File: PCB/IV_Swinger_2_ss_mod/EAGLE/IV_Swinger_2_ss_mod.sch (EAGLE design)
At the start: 33 parts, among them J1 

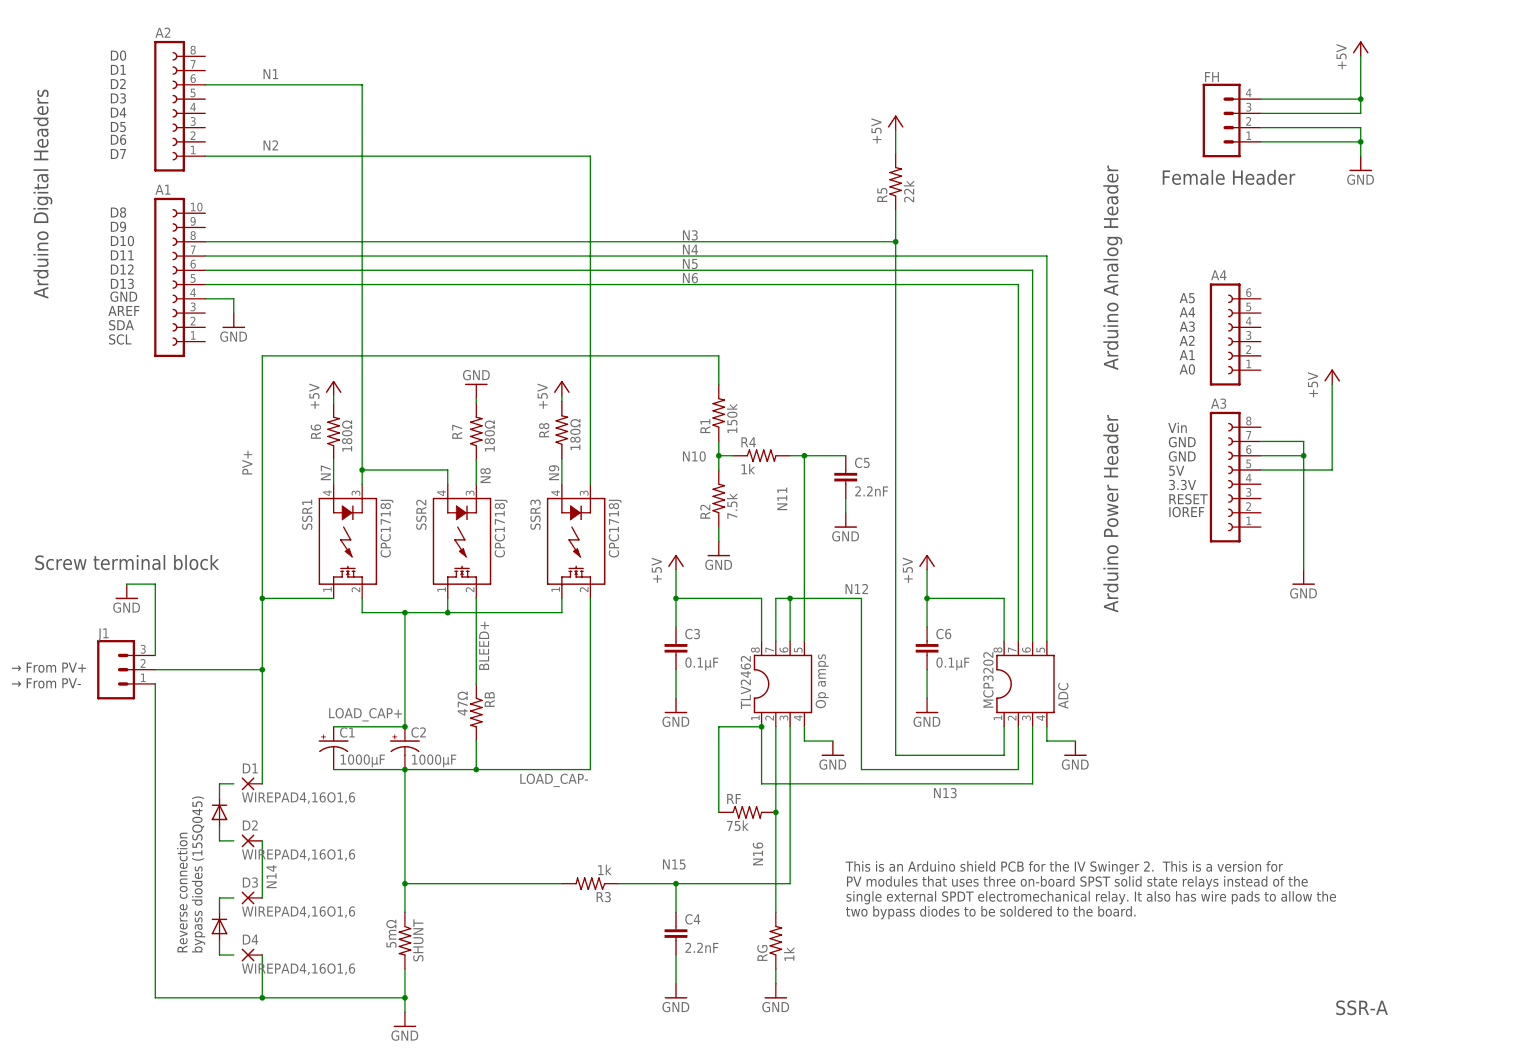
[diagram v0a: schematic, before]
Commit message: SSR module version PCB, RevB
Fixed bugs in RevA of the SSR module version PCB:

Issue #40: Must drive SSR1 and SSR2 from separate Arduino pins. In the RevA design, there is a path from +5V to GND through the two SSRs, which can cause destruction of the SSRs and the bleed resistor.

Issue #41: Resistor R3 must be connected precisely to the shunt (+) end pad so it doesn't see the voltage at some point in the sea of copper that is the LOAD_CAP- net.  This resulted in current measurements that were too high, and depended on whether the current was flowing from SSR3 or from the load caps.

Issue #41: The path from the shunt (-) end pad to the screw terminal pads must be a stub off the GND plane so that when current is flowing, the GND plane doesn't see a voltage drop.  Also, the linkage between this stub and the GND plane must be made at the shunt (-) end pad so the voltage of the GND plane is equal to the voltage at the (-) end of the shunt.

Also swapped the pads for the bypass diodes for layout reasons related to making the current-carrying part of GND a stub.
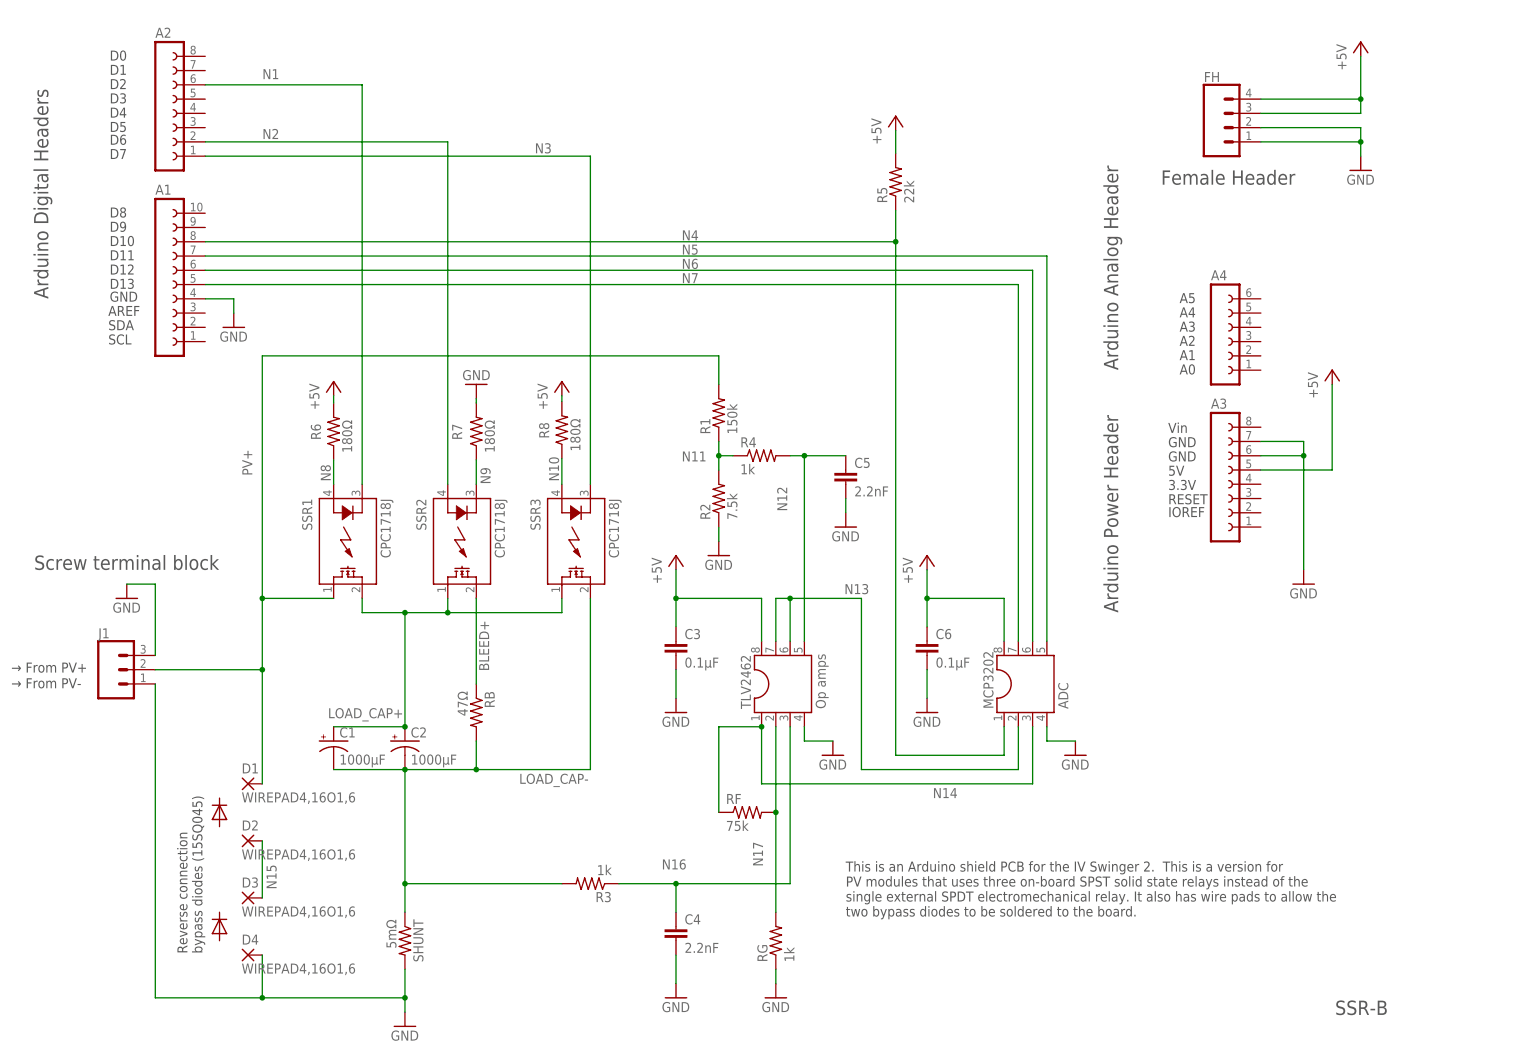
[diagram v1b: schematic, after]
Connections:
- new net N17: RF.2, RG.2, TLV2462.2
- net N1: no longer SSR2.A
- net N10: now also R8.1, SSR3.A; no longer R1.1, R2.2, R4.1
- net N11: now also R1.1, R2.2, R4.1; no longer C5.1, R4.2, TLV2462.5
- net N12: now also C5.1, R4.2, TLV2462.5; no longer MCP3202.2, TLV2462.6, TLV2462.7
- net N13: now also MCP3202.2, TLV2462.6, TLV2462.7; no longer MCP3202.3, RF.1, TLV2462.1
- net N14: now also MCP3202.3, RF.1, TLV2462.1; no longer D2.P, D3.P
- net N15: now also D2.P, D3.P; no longer C4.1, R3.1, TLV2462.3
- net N16: now also C4.1, R3.1, TLV2462.3; no longer RF.2, RG.2, TLV2462.2
- net N2: now also A2.2, SSR2.A; no longer A2.1, SSR3.K
- net N3: now also A2.1, SSR3.K; no longer A1.8, MCP3202.1, R5.1
- net N4: now also A1.8, MCP3202.1, R5.1; no longer A1.7, MCP3202.5
- net N5: now also A1.7, MCP3202.5; no longer A1.6, MCP3202.6
- net N6: now also A1.6, MCP3202.6; no longer A1.5, MCP3202.7
- net N7: now also A1.5, MCP3202.7; no longer R6.1, SSR1.A
- net N8: now also R6.1, SSR1.A; no longer R7.1, SSR2.K
- net N9: now also R7.1, SSR2.K; no longer R8.1, SSR3.A
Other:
- note added: "SSR-B"
- note removed: "SSR-A"
